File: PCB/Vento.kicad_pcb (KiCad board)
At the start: 4 copper layers, 81 x 27 mm, 96 parts, among them J1 B2B-PH-K-S(LF)(SN), J2 B3B-PH-K-S(LF)(SN), J3 20021121-00010C4LF, J4 0475890001-MicroUSBPort, P1 CONN_01X18, P2 CONN_01X18, Q1 DMG2307L-7, Q2 DMG2307L-7, SW1 B3U-1000P, SW2 B3U-1000P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

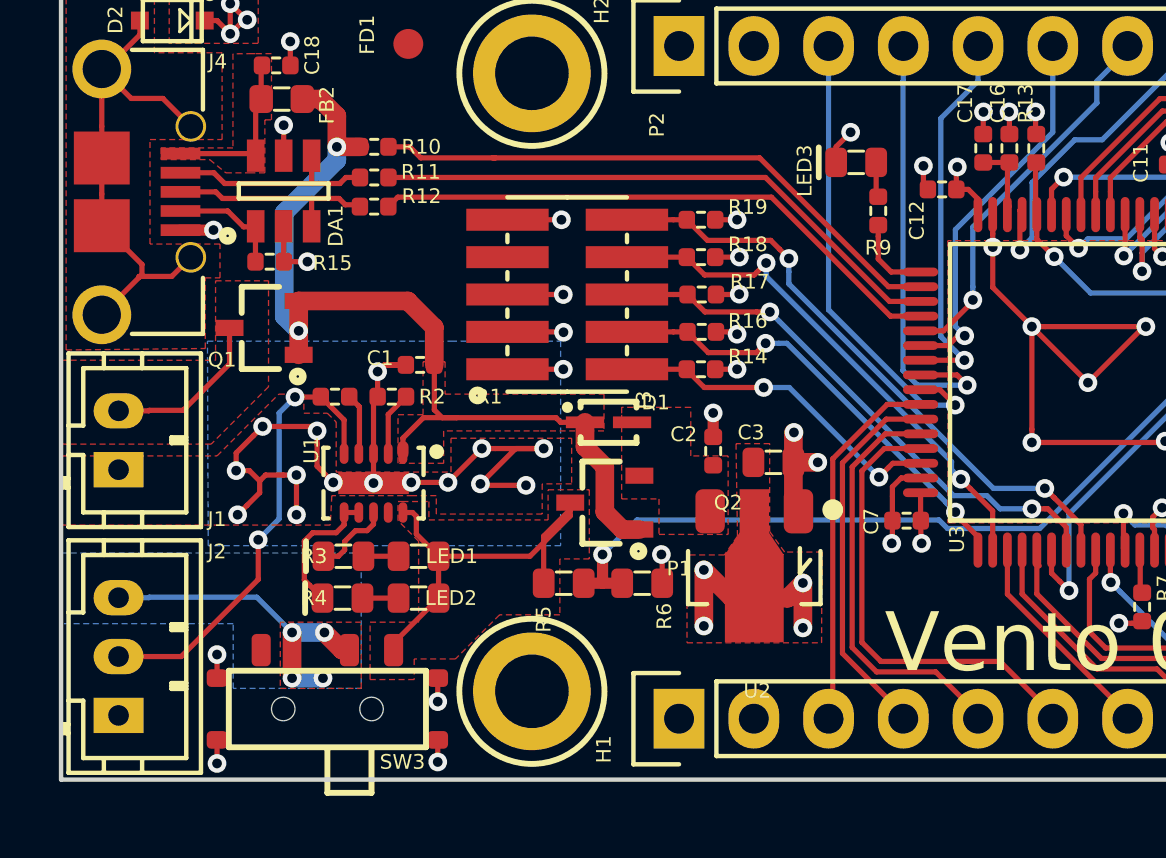
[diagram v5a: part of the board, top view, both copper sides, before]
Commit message: New Power Topology
LDO swapped for one with a shutdown enable from Microchip. On/Off
switchnow toggles the shutdown enable from the new LDO.
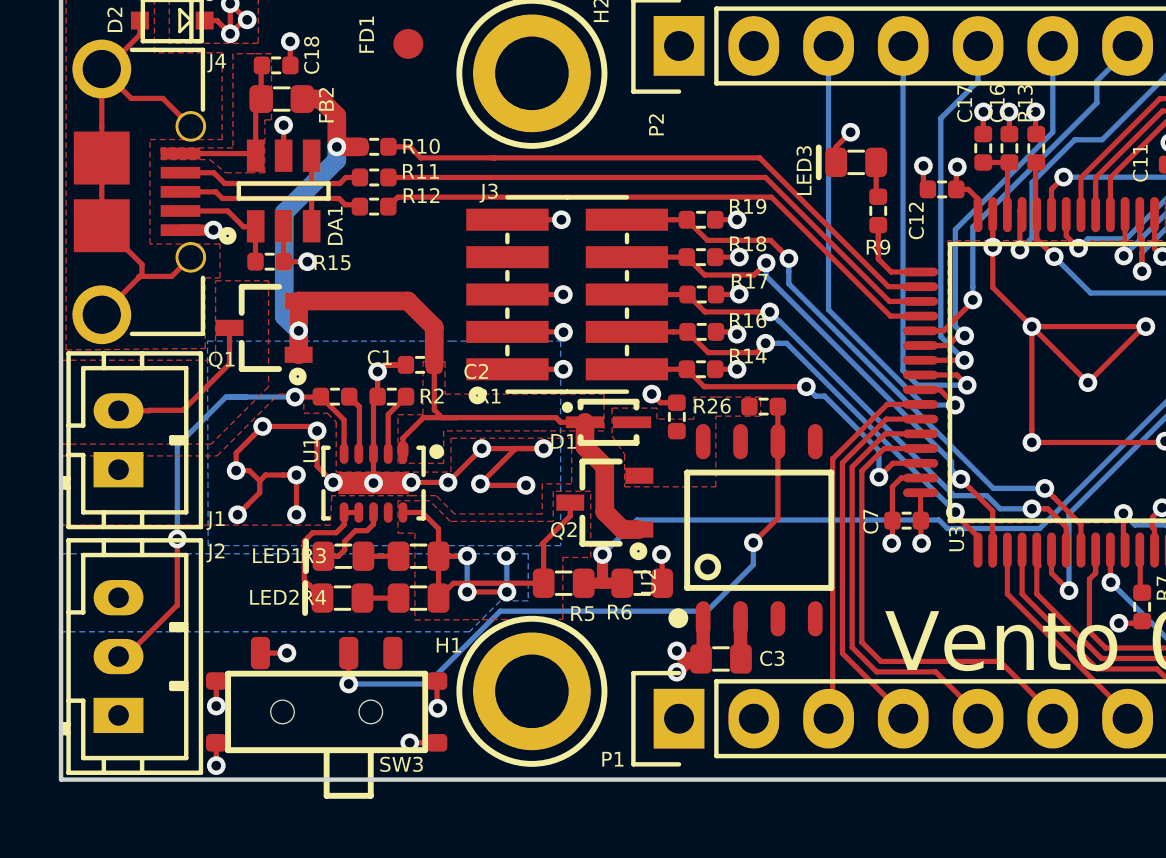
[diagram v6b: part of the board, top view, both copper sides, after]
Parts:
- added R26: RC1005F103CS, PCB_Footprints:R0402, F.Cu at (168.7, 85.9)
- U2: value AZ1117CR-3.3TRG1_1 -> TC1265-3.3VOA; footprint PCB_Footprints:AZ1117CR-3.3TRG1 -> PCB_Footprints:TC1265-3.3VOA
- moved C3 6.91 mm to (167.3, 94.5)
- moved C2 1.69 mm to (165.8, 86.3)
- moved U2 1.22 mm to (168.6, 90.1), turned to 90 degrees
- moved SW3 0.10 mm to (153.9, 96.3)
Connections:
- C2 pad 1: Net-(C2-Pad1) -> /Power/LDO_VIN
- D1 pad 2: Net-(C2-Pad1) -> /Power/LDO_VIN
- J2 pad 3: Net-(J2-Pad3) -> /Power/BAT
- Q2 pad 2: Net-(C2-Pad1) -> /Power/LDO_VIN
- SW3 pad 1: Net-(SW3-Pad1) -> GND
- SW3 pad 2: Net-(J2-Pad3) -> Net-(R26-Pad2)
- SW3 pad 3: /Power/BAT -> Net-(SW3-Pad3)
- U2 pad 1: GND -> +3V3
- U2 pad 2: +3V3 -> GND
- U2 pad 3: Net-(C2-Pad1) -> Net-(U2-Pad3)
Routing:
- net Net-(R26-Pad2): track 0.00 -> 22.2 mm, vias 0 -> 2
- net Net-(J2-Pad3): track 11.2 -> 0.00 mm, vias 4 -> 0
- net +3V3: track 54.6 -> 50.6 mm, vias 24 -> 22
- net GND: track 315.0 -> 314.0 mm, vias 185 -> 184
- net /Power/BAT: track 14.6 -> 15.5 mm, vias 0 -> 4
- net /Power/THERM: track 15.7 -> 16.6 mm
- added copper zone on B.Cu, net /Power/BAT
- added copper zone on F.Cu, net /Power/LDO_VIN
- removed copper zone on F.Cu, net +3V3
- removed copper zone on F.Cu, net Net-(C2-Pad1)
- removed copper zone on B.Cu, net Net-(J2-Pad3)
- removed copper zone on F.Cu, net Net-(J2-Pad3)
